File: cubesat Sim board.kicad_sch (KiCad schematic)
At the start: 37 parts, among them J1 HASP Power In, J10 USB_2_OUT, J2 PI Bus, J3 JST_Solar, J4 JST_Main(optional), J5 INA219, J6 HASP Data In, J7 USB_IN, J8 USB_2, J9 USB_1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

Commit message: BOM
Updated BOMs
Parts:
- X1: now left out of the parts list
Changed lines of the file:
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@@
 		(unit 1)
 		(exclude_from_sim no)
-		(in_bom yes)
+		(in_bom no)
 		(on_board yes)
 		(dnp no)

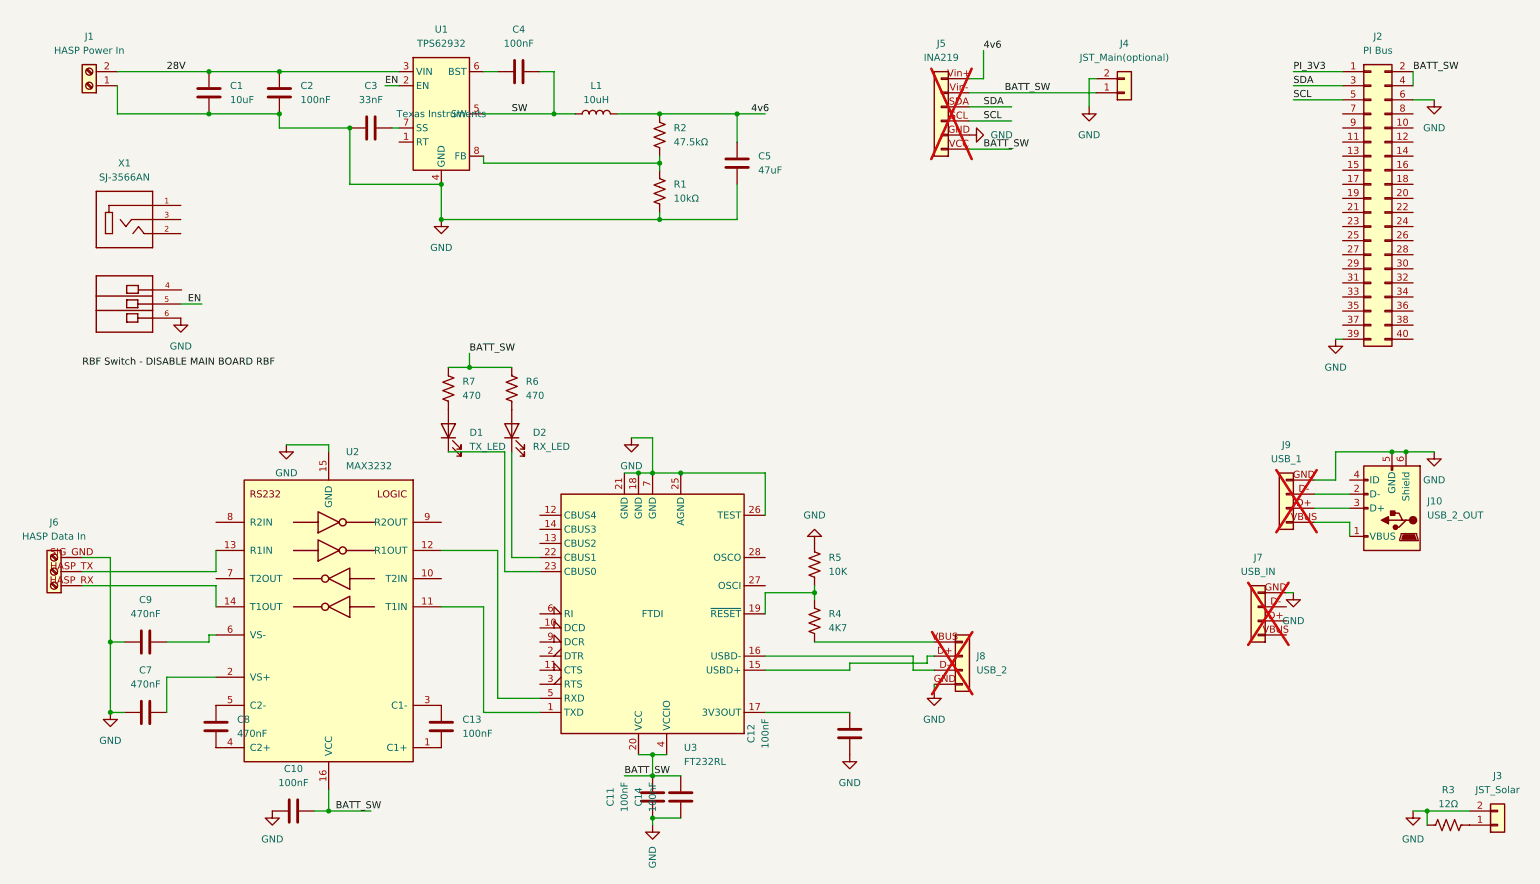
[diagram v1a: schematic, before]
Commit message: Fixes to some ERC checks. Tracking down a potential short issue.
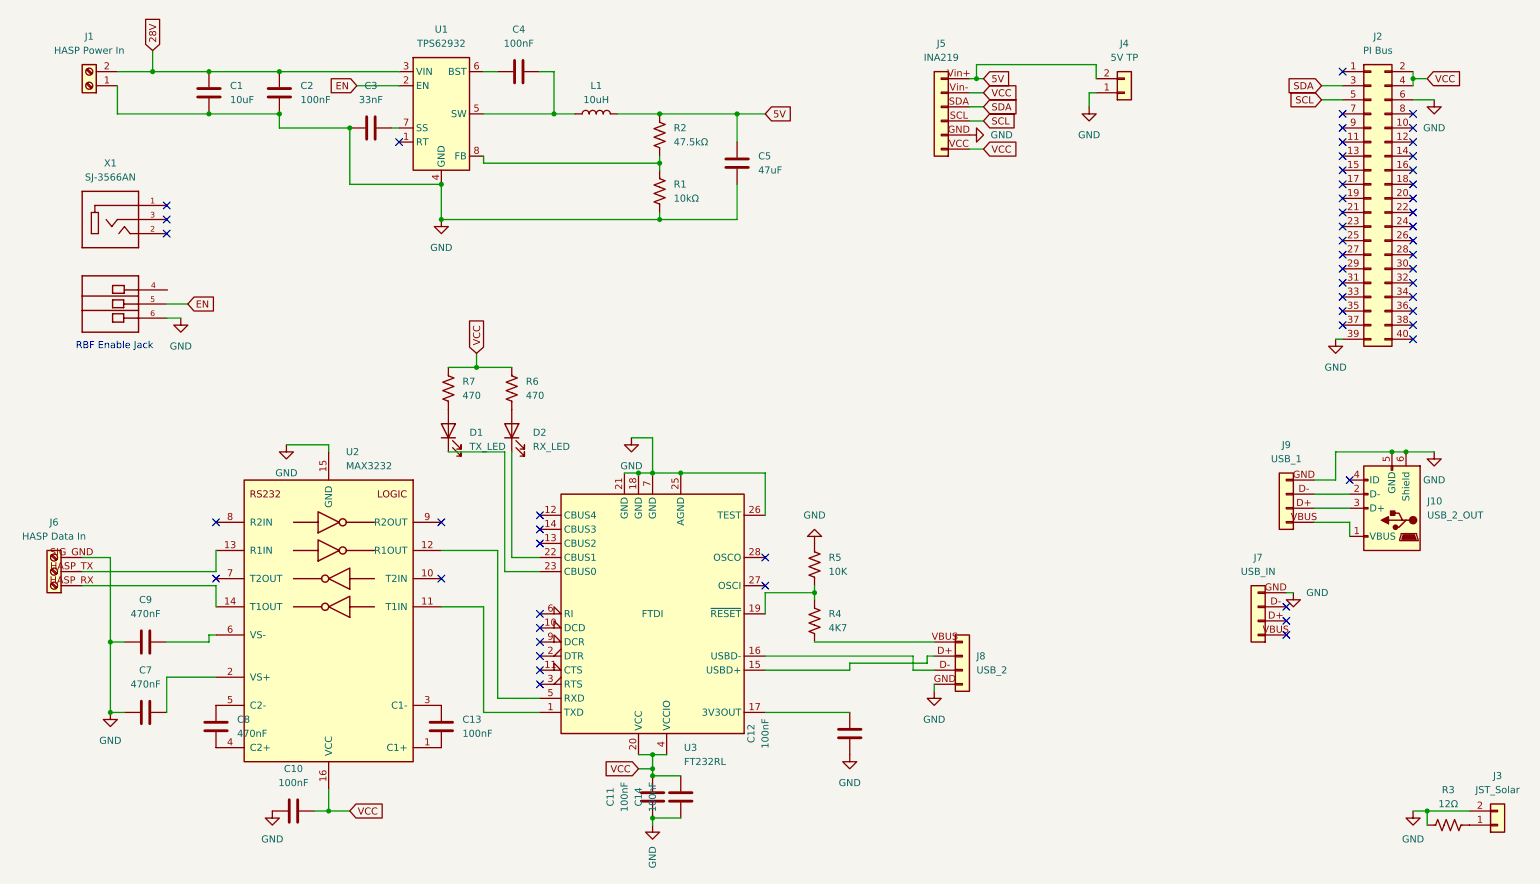
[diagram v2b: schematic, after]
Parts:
- J4: value JST_Main(optional) -> 5V TP
- J5, J7, J8, J9: now fitted
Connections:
- net GND: now also J4.1 (Pin_1); no longer J4.2 (Pin_2)
- net 4v6 renamed 5V
- net 5V: now also J4.2 (Pin_2)
- net BATT_SW renamed VCC
- net VCC: no longer J4.1 (Pin_1)
- net PI_3V3: no longer names the net of J2.1 (Pin_1)
- net SW: no longer names the net of C4.2, L1.1, U1.5 (SW)
- no-connect marks 0 -> 57
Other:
- note added: "RBF Enable Jack"
- moved on the sheet: X1
